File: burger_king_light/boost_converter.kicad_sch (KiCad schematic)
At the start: 14 parts, among them IC1 TPS55340PWPR

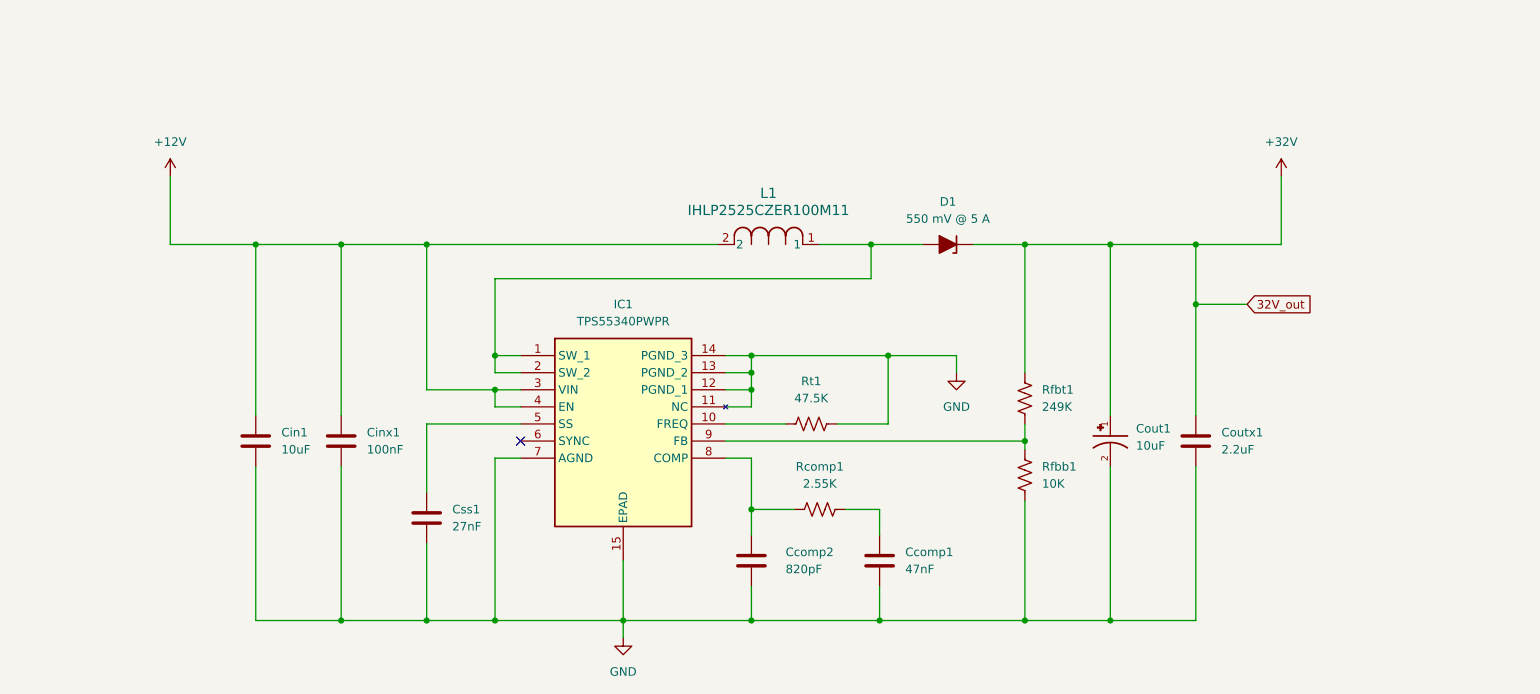
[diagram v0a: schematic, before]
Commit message: updated all components for 36V operation
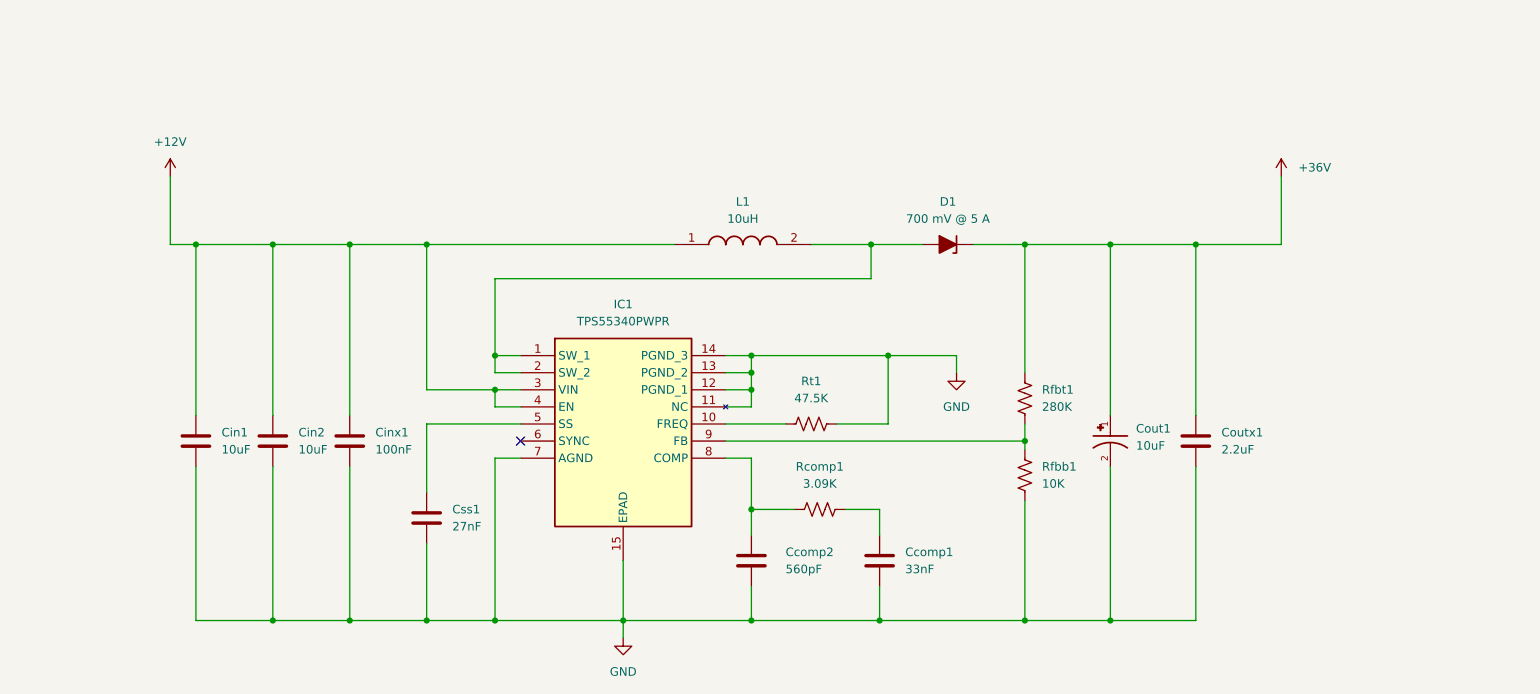
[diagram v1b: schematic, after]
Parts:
- removed L1: IHLP2525CZER100M11, IND_IHLP_2525_CZ_VIS, symbol passives:IHLP2525CZER100M11
- added Cin1: 10uF, Capacitor_SMD:C_1812_4532Metric, symbol Device:C
- added L1: 10uH, INDPM125125X450N, symbol passives:PM124SH-100M-RC
- Ccomp1: value 47nF -> 33nF; Part Number GRM31M5C1H473JA01L -> C1206C333F5GEC7210
- Ccomp2: value 820pF -> 560pF; footprint Capacitor_SMD:C_0805_2012Metric -> Capacitor_SMD:C_1206_3216Metric; Part Number GRM2165C2A821JA01D -> KGM31BCG2A561JT
- D1: value 550 mV @ 5 A -> 700 mV @ 5 A; footprint Diode_SMD:D_SMA -> Diode_SMD:D_SMC; Part Number CDBA540-HF -> B560CQ-13-F
- Rcomp1: value 2.55K -> 3.09K; Part Number RC1206FR-072K55L -> ERA-8AEB3091V
- Rfbt1: value 249K -> 280K; Part Number CRCW1206249KFKEA -> RQ73C2B280KBTD
- renumbered Cin1 to Cin2
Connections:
- net +12V: now also Cin1.1, L1.1
- net GND: now also Cin1.2
- net at D1.2 (A), IC1.1 (SW_1), IC1.2 (SW_2): now also L1.2
- net +32V renamed +36V
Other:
- moved on the sheet: Cin2, Cinx1

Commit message: added footprints for DNP snubbers; redesigned output capacitance; added bulk capacitance for PWM switching
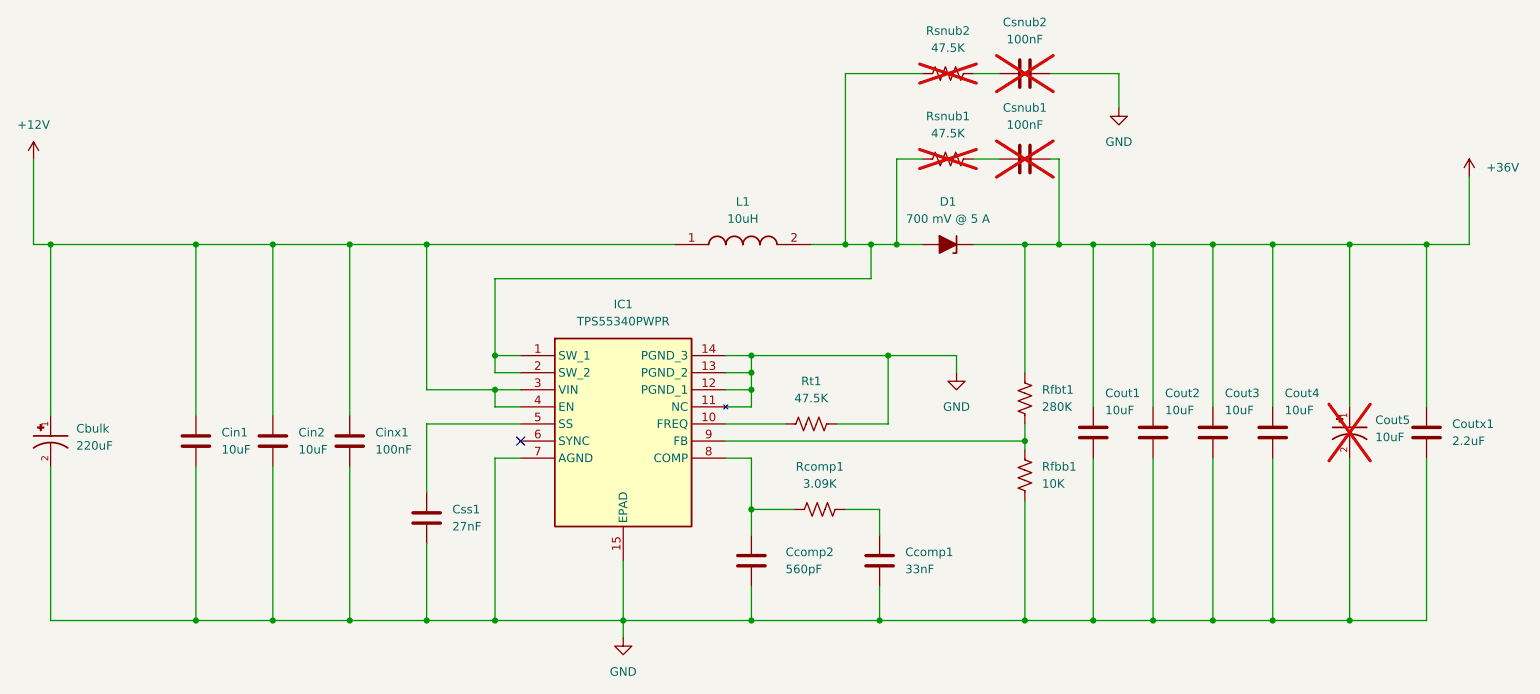
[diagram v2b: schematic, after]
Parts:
- added Cbulk: 220uF, Capacitor_THT:CP_Radial_D8.0mm_P3.50mm, symbol passives:EEHZA1H100R
- added Cout1, Cout2, Cout3, Cout4: 10uF, Capacitor_SMD:C_1812_4532Metric, symbol Device:C
- added Csnub1, Csnub2: 100nF, Capacitor_SMD:C_0805_2012Metric, symbol Device:C
- added Rsnub1, Rsnub2: 47.5K, Resistor_SMD:R_1206_3216Metric, symbol Device:R_US
- Cin1, Cin2: Part Number CGA8P2X7R1E106K250KA -> C1812X106K050T
- Cout5: renamed from Cout1; now not fitted
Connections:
- net +12V: now also Cbulk.1
- net +36V: now also Cout1.1, Cout2.1, Cout3.1, Cout4.1, Csnub1.2
- net GND: now also Cbulk.2, Cout1.2, Cout2.2, Cout3.2, Cout4.2, Csnub2.2
- net at D1.2 (A), IC1.1 (SW_1), IC1.2 (SW_2)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: now also Rsnub1.2, Rsnub2.2
- new net: Csnub2.1, Rsnub2.1
- new net: Csnub1.1, Rsnub1.1
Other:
- moved on the sheet: Coutx1

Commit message: reassigned reference designations
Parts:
- renumbered Cbulk to Cbulk1, Ccomp2 to Ccomp1, Ccomp1 to Ccomp2, Csnub2 to Csnub1, Csnub1 to Csnub2, Rsnub2 to Rsnub1, Rsnub1 to Rsnub2
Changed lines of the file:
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@@
 		(dnp yes)
 		(fields_autoplaced yes)
-		(property "Reference" "Csnub2"
+		(property "Reference" "Csnub1"
 			(at 196.85 46.99 90)
 			(show_name no)
@@
 			(project "burger_king_light"
 				(path "/a1df17e6-efc5-454a-8f2a-f09b9061eebb/2b973585-e867-4f75-9aeb-d45cf169fa75"
-					(reference "Csnub2")
+					(reference "Csnub1")
 					(unit 1)
 				)
@@
 		(dnp yes)
 		(fields_autoplaced yes)
-		(property "Reference" "Rsnub2"
+		(property "Reference" "Rsnub1"
 			(at 185.42 48.26 90)
 			(show_name no)
@@
 			(project "burger_king_light"
 				(path "/a1df17e6-efc5-454a-8f2a-f09b9061eebb/2b973585-e867-4f75-9aeb-d45cf169fa75"
-					(reference "Rsnub2")
+					(reference "Rsnub1")
 					(unit 1)
 				)
@@
 		(dnp no)
 		(fields_autoplaced yes)
-		(property "Reference" "#PWR09"
+		(property "Reference" "#PWR06"
 			(at 210.82 66.04 0)
 			(hide yes)
@@
 			(project "burger_king_light"
 				(path "/a1df17e6-efc5-454a-8f2a-f09b9061eebb/2b973585-e867-4f75-9aeb-d45cf169fa75"
-					(reference "#PWR09")
+					(reference "#PWR06")
 					(unit 1)
 				)
@@
 		(dnp no)
 		(fields_autoplaced yes)
-		(property "Reference" "#PWR04"
+		(property "Reference" "#PWR05"
 			(at 186.69 105.41 0)
 			(hide yes)
@@
 			(project "burger_king_light"
 				(path "/a1df17e6-efc5-454a-8f2a-f09b9061eebb/2b973585-e867-4f75-9aeb-d45cf169fa75"
-					(reference "#PWR04")
+					(reference "#PWR05")
 					(unit 1)
 				)
@@
 		(dnp yes)
 		(fields_autoplaced yes)
-		(property "Reference" "Csnub1"
+		(property "Reference" "Csnub2"
 			(at 196.85 59.69 90)
 			(show_name no)
@@
 			(project "burger_king_light"
 				(path "/a1df17e6-efc5-454a-8f2a-f09b9061eebb/2b973585-e867-4f75-9aeb-d45cf169fa75"
-					(reference "Csnub1")
+					(reference "Csnub2")
 					(unit 1)
 				)
@@
 		(dnp no)
 		(fields_autoplaced yes)
-		(property "Reference" "Ccomp1"
+		(property "Reference" "Ccomp2"
 			(at 179.07 125.7299 0)
 			(show_name no)
@@
 			(project "burger_king_light"
 				(path "/a1df17e6-efc5-454a-8f2a-f09b9061eebb/2b973585-e867-4f75-9aeb-d45cf169fa75"
-					(reference "Ccomp1")
+					(reference "Ccomp2")
 					(unit 1)
 				)
@@
 		(dnp yes)
 		(fields_autoplaced yes)
-		(property "Reference" "Rsnub1"
+		(property "Reference" "Rsnub2"
 			(at 185.42 60.96 90)
 			(show_name no)
@@
 			(project "burger_king_light"
 				(path "/a1df17e6-efc5-454a-8f2a-f09b9061eebb/2b973585-e867-4f75-9aeb-d45cf169fa75"
-					(reference "Rsnub1")
+					(reference "Rsnub2")
 					(unit 1)
 				)
@@
 		(in_pos_files yes)
 		(dnp no)
-		(property "Reference" "Ccomp2"
+		(property "Reference" "Ccomp1"
 			(at 161.29 125.7299 0)
 			(show_name no)
@@
 			(project "burger_king_light"
 				(path "/a1df17e6-efc5-454a-8f2a-f09b9061eebb/2b973585-e867-4f75-9aeb-d45cf169fa75"
-					(reference "Ccomp2")
+					(reference "Ccomp1")
 					(unit 1)
 				)
@@
 		(dnp no)
 		(fields_autoplaced yes)
-		(property "Reference" "#PWR03"
+		(property "Reference" "#PWR04"
 			(at 137.16 144.78 0)
 			(hide yes)
@@
 			(project "burger_king_light"
 				(path "/a1df17e6-efc5-454a-8f2a-f09b9061eebb/2b973585-e867-4f75-9aeb-d45cf169fa75"
-					(reference "#PWR03")
+					(reference "#PWR04")
 					(unit 1)
 				)
@@
 		(dnp no)
 		(fields_autoplaced yes)
-		(property "Reference" "Cbulk"
+		(property "Reference" "Cbulk1"
 			(at 55.88 107.3765 90)
 			(show_name no)
@@
 			(project "burger_king_light"
 				(path "/a1df17e6-efc5-454a-8f2a-f09b9061eebb/2b973585-e867-4f75-9aeb-d45cf169fa75"
-					(reference "Cbulk")
+					(reference "Cbulk1")
 					(unit 1)
 				)
@@
 		(dnp no)
 		(fields_autoplaced yes)
-		(property "Reference" "#PWR01"
+		(property "Reference" "#PWR03"
 			(at 49.53 71.12 0)
 			(hide yes)
@@
 			(project "burger_king_light"
 				(path "/a1df17e6-efc5-454a-8f2a-f09b9061eebb/2b973585-e867-4f75-9aeb-d45cf169fa75"
-					(reference "#PWR01")
+					(reference "#PWR03")
 					(unit 1)
 				)
@@
 		(dnp no)
 		(fields_autoplaced yes)
-		(property "Reference" "#PWR02"
+		(property "Reference" "#PWR07"
 			(at 262.89 73.66 0)
 			(hide yes)
@@
 			(project "burger_king_light"
 				(path "/a1df17e6-efc5-454a-8f2a-f09b9061eebb/2b973585-e867-4f75-9aeb-d45cf169fa75"
-					(reference "#PWR02")
-					(unit 1)
-				)
+					(reference "#PWR07")
+					(unit 1)
+				)

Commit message: changed IC reference designators to U
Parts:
- Cout5: footprint EEHZA1H100R:CAP_EEHZA1H100R -> Capacitor_SMD:CP_Elec_5x5.3
- renumbered IC1 to U1
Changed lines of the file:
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@@
 			)
 		)
-		(property "Footprint" "EEHZA1H100R:CAP_EEHZA1H100R"
+		(property "Footprint" "Capacitor_SMD:CP_Elec_5x5.3"
 			(at 245.11 106.68 0)
 			(hide yes)
@@
 		(dnp no)
 		(fields_autoplaced yes)
-		(property "Reference" "IC1"
+		(property "Reference" "U1"
 			(at 137.16 88.9 0)
 			(show_name no)
@@
 			(project "burger_king_light"
 				(path "/a1df17e6-efc5-454a-8f2a-f09b9061eebb/2b973585-e867-4f75-9aeb-d45cf169fa75"
-					(reference "IC1")
+					(reference "U1")
 					(unit 1)
 				)

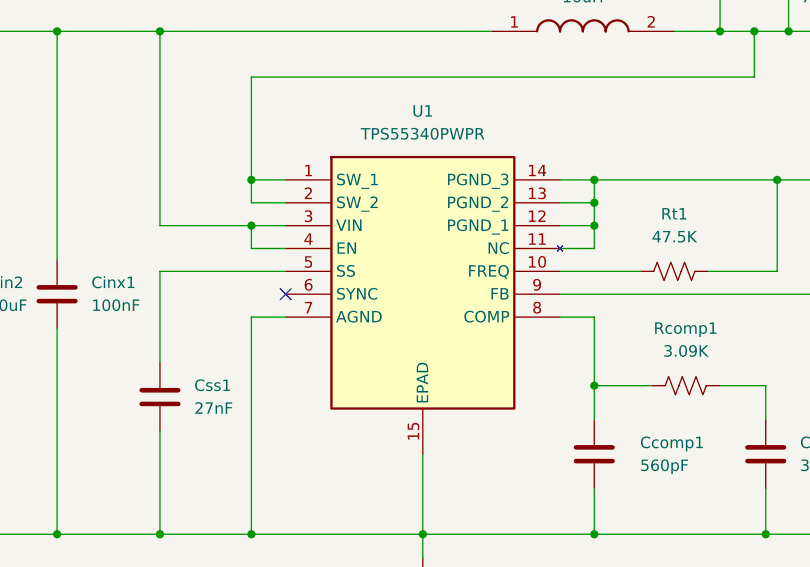
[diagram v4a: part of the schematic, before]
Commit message: renamed some ICs, fixed DNP flags
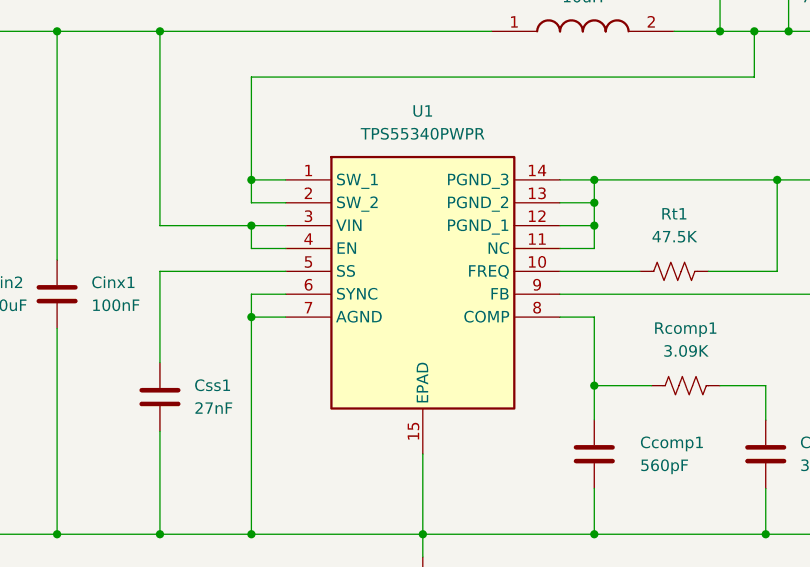
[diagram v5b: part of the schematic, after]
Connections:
- net GND: now also U1.6 (SYNC)
- no-connect marks 1 -> 0
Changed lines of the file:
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@@
+	)
+	(junction
+		(at 118.11 111.76)
+		(diameter 0)
+		(color 0 0 0 0)
 	)
 	(junction
@@
 		(color 0 0 0 0)
 	)
-	(no_connect
-		(at 121.92 109.22)
-	)
 	(wire
 		(pts
@@
 	(wire
 		(pts
+			(xy 118.11 109.22) (xy 118.11 111.76)
+		)
+		(stroke
+			(width 0)
+			(type default)
+		)
+	)
+	(wire
+		(pts
 			(xy 152.4 104.14) (xy 156.21 104.14)
 		)
@@
 		)
 		(stroke
+			(width 0)
+			(type default)
+		)
+	)
+	(wire
+		(pts
+			(xy 121.92 109.22) (xy 118.11 109.22)
+		)
+		(stroke
